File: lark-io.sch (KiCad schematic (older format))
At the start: 30 parts

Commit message: Finalize schematic
Finish part selection

Pending issues: IMU, switches & LEDs, mechanical parts and housing
selection.
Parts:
- C40, C41, C42, C43, C44, C45, C46, C50: renamed from C?; footprint (none) -> Capacitor_SMD:C_0805_2012Metric_Pad1.15x1.40mm_HandSolder; MPN (none) -> 885012207128
- C47: renamed from C?; footprint (none) -> Capacitor_SMD:CP_Elec_16x17.5; MPN (none) -> 493-16063-1-ND
- C48, C49: renamed from C?; footprint (none) -> Capacitor_SMD:C_0805_2012Metric_Pad1.15x1.40mm_HandSolder; MPN (none) -> 885012207102
- F1, F2: renamed from F?; value Polyfuse -> 1.25A/16V; footprint (none) -> Fuse:Fuse_1812_4532Metric_Pad1.30x3.40mm_HandSolder; MPN (none) -> 1812L125/16DR
- J6: renamed from J?; value Conn_01x05 -> UART1; footprint (none) -> Connector_PinHeader_2.54mm:PinHeader_1x05_P2.54mm_Vertical
- J9: renamed from J?; value Conn_01x04 -> SOUND; footprint (none) -> Connector_PinHeader_2.54mm:PinHeader_1x04_P2.54mm_Vertical
- R27, R28, R29, R30, R31, R32: renamed from R?; footprint (none) -> Resistor_SMD:R_0805_2012Metric_Pad1.15x1.40mm_HandSolder; MPN (none) -> RC0805FR-07470RL
- R33, R34: renamed from R?; footprint (none) -> Resistor_SMD:R_0805_2012Metric_Pad1.15x1.40mm_HandSolder; MPN (none) -> RC0805FR-0710KL
- R35, R36: renamed from R?; footprint (none) -> Resistor_SMD:R_0805_2012Metric_Pad1.15x1.40mm_HandSolder; MPN (none) -> RC0805FR-071KL
- U10: renamed from U?; footprint (none) -> Package_SO:SOIC-16_3.9x9.9mm_P1.27mm; MPN (none) -> MAX3232ECDR
- U11: renamed from U?; footprint (none) -> Package_SO:SOIC-16_3.9x9.9mm_P1.27mm; MPN (none) -> PAM8403DR
- gave numbers to parts that had none: 3
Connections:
- no-connect marks 6 -> 7

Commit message: Replace MPU-9250 IMU with BMX055
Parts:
- renumbered C40 to C39, C41 to C40, C42 to C41, C43 to C42, C44 to C43, C45 to C44, C46 to C45, C47 to C46, C48 to C47, C49 to C48, C50 to C49
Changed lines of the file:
@@
 Connection ~ 3750 7200
 $Comp
-L Device:C C42
+L Device:C C41
 U 1 1 5C55CA57
 P 6000 1850
-F 0 "C42" H 6115 1896 50  0000 L CNN
+F 0 "C41" H 6115 1896 50  0000 L CNN
 F 1 "100n" H 6115 1805 50  0000 L CNN
 F 2 "Capacitor_SMD:C_0805_2012Metric_Pad1.15x1.40mm_HandSolder" H 6038 1700 50  0001 C CNN
@@
 $EndComp
 $Comp
-L Device:C C41
+L Device:C C40
 U 1 1 5C55CA9D
 P 3600 1850
-F 0 "C41" H 3715 1896 50  0000 L CNN
+F 0 "C40" H 3715 1896 50  0000 L CNN
 F 1 "100n" H 3715 1805 50  0000 L CNN
 F 2 "Capacitor_SMD:C_0805_2012Metric_Pad1.15x1.40mm_HandSolder" H 3638 1700 50  0001 C CNN
@@
 $EndComp
 $Comp
-L Device:C C40
+L Device:C C39
 U 1 1 5C55CAEA
 P 5250 1000
-F 0 "C40" H 5365 1046 50  0000 L CNN
+F 0 "C39" H 5365 1046 50  0000 L CNN
 F 1 "100n" H 5365 955 50  0000 L CNN
 F 2 "Capacitor_SMD:C_0805_2012Metric_Pad1.15x1.40mm_HandSolder" H 5288 850 50  0001 C CNN
@@
 $EndComp
 $Comp
-L Device:C C43
+L Device:C C42
 U 1 1 5C55CCBE
 P 6400 2200
-F 0 "C43" V 6148 2200 50  0000 C CNN
+F 0 "C42" V 6148 2200 50  0000 C CNN
 F 1 "100n" V 6239 2200 50  0000 C CNN
 F 2 "Capacitor_SMD:C_0805_2012Metric_Pad1.15x1.40mm_HandSolder" H 6438 2050 50  0001 C CNN
@@
 $EndComp
 $Comp
-L Device:C C44
+L Device:C C43
 U 1 1 5C55CF99
 P 6400 2600
-F 0 "C44" V 6148 2600 50  0000 C CNN
+F 0 "C43" V 6148 2600 50  0000 C CNN
 F 1 "100n" V 6239 2600 50  0000 C CNN
 F 2 "Capacitor_SMD:C_0805_2012Metric_Pad1.15x1.40mm_HandSolder" H 6438 2450 50  0001 C CNN
@@
 	3400 4850 3400 5300
 $Comp
-L Device:C C45
+L Device:C C44
 U 1 1 5C5B142F
 P 3050 5100
-F 0 "C45" H 3165 5146 50  0000 L CNN
+F 0 "C44" H 3165 5146 50  0000 L CNN
 F 1 "100n" H 3165 5055 50  0000 L CNN
 F 2 "Capacitor_SMD:C_0805_2012Metric_Pad1.15x1.40mm_HandSolder" H 3088 4950 50  0001 C CNN
@@
 $EndComp
 $Comp
-L Device:C C46
+L Device:C C45
 U 1 1 5C5B14AD
 P 4050 5100
-F 0 "C46" H 4165 5146 50  0000 L CNN
+F 0 "C45" H 4165 5146 50  0000 L CNN
 F 1 "100n" H 4165 5055 50  0000 L CNN
 F 2 "Capacitor_SMD:C_0805_2012Metric_Pad1.15x1.40mm_HandSolder" H 4088 4950 50  0001 C CNN
@@
 $EndComp
 $Comp
-L Device:CP C47
+L Device:CP C46
 U 1 1 5C5BC765
 P 4500 5100
-F 0 "C47" H 4618 5146 50  0000 L CNN
+F 0 "C46" H 4618 5146 50  0000 L CNN
 F 1 "470u" H 4618 5055 50  0000 L CNN
 F 2 "Capacitor_SMD:CP_Elec_16x17.5" H 4538 4950 50  0001 C CNN
@@
 	3050 5250 3050 5350
 $Comp
-L Device:C C48
+L Device:C C47
 U 1 1 5C5FA3E9
 P 2450 5900
-F 0 "C48" V 2198 5900 50  0000 C CNN
+F 0 "C47" V 2198 5900 50  0000 C CNN
 F 1 "470n" V 2289 5900 50  0000 C CNN
 F 2 "Capacitor_SMD:C_0805_2012Metric_Pad1.15x1.40mm_HandSolder" H 2488 5750 50  0001 C CNN
@@
 $EndComp
 $Comp
-L Device:C C49
+L Device:C C48
 U 1 1 5C5FA49A
 P 1900 6200
-F 0 "C49" V 1648 6200 50  0000 C CNN
+F 0 "C48" V 1648 6200 50  0000 C CNN
 F 1 "470n" V 1739 6200 50  0000 C CNN
 F 2 "Capacitor_SMD:C_0805_2012Metric_Pad1.15x1.40mm_HandSolder" H 1938 6050 50  0001 C CNN
@@
 Connection ~ 2750 6350
 $Comp
-L Device:C C50
+L Device:C C49
 U 1 1 5C605E58
 P 2650 6900
-F 0 "C50" H 2765 6946 50  0000 L CNN
+F 0 "C49" H 2765 6946 50  0000 L CNN
 F 1 "100n" H 2765 6855 50  0000 L CNN
 F 2 "Capacitor_SMD:C_0805_2012Metric_Pad1.15x1.40mm_HandSolder" H 2688 6750 50  0001 C CNN

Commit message: Intermediate status while arranging compontents.
Manually grouped components into smaller islands.

Some parts were changed:
* U1: SOT-23-3 LDO should be sufficient
* CP_Elec: Use 10x10 size
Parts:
- C46: footprint Capacitor_SMD:CP_Elec_16x17.5 -> Capacitor_SMD:CP_Elec_10x10
- CON1: symbol dk_Barrel-Audio-Connectors:SJ1-3523N -> lark-rescue:SJ1-3523N-dk_Barrel-Audio-Connectors
- J7, J8: symbol dk_Modular-Connectors-Jacks:54602-908LF -> lark-rescue:54602-908LF-dk_Modular-Connectors-Jacks
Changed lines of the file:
@@
 $EndComp
 $Comp
-L dk_Modular-Connectors-Jacks:54602-908LF J7
+L lark-rescue:54602-908LF-dk_Modular-Connectors-Jacks J7
 U 1 1 5C6D6815
 P 9150 2050
+AR Path="/5C6D6815" Ref="J7"  Part="1"
+AR Path="/5C549AF9/5C6D6815" Ref="J7"  Part="1"
 F 0 "J7" V 9246 1595 50  0000 R CNN
 F 1 "54602-908LF" V 9155 1595 50  0000 R CNN
@@
 $EndComp
 $Comp
-L dk_Modular-Connectors-Jacks:54602-908LF J8
+L lark-rescue:54602-908LF-dk_Modular-Connectors-Jacks J8
 U 1 1 5C6D6947
 P 9150 3550
+AR Path="/5C6D6947" Ref="J8"  Part="1"
+AR Path="/5C549AF9/5C6D6947" Ref="J8"  Part="1"
 F 0 "J8" V 9246 3095 50  0000 R CNN
 F 1 "54602-908LF" V 9155 3095 50  0000 R CNN
@@
 $EndComp
 $Comp
-L dk_Barrel-Audio-Connectors:SJ1-3523N CON1
+L lark-rescue:SJ1-3523N-dk_Barrel-Audio-Connectors CON1
 U 1 1 5C55B74E
 P 5600 6900
+AR Path="/5C55B74E" Ref="CON1"  Part="1"
+AR Path="/5C549AF9/5C55B74E" Ref="CON1"  Part="1"
 F 0 "CON1" H 5273 6953 60  0000 R CNN
 F 1 "SJ1-3523N" H 5273 6847 60  0000 R CNN
@@
 F 0 "C46" H 4618 5146 50  0000 L CNN
 F 1 "470u" H 4618 5055 50  0000 L CNN
-F 2 "Capacitor_SMD:CP_Elec_16x17.5" H 4538 4950 50  0001 C CNN
+F 2 "Capacitor_SMD:CP_Elec_10x10" H 4538 4950 50  0001 C CNN
 F 3 "~" H 4500 5100 50  0001 C CNN
 F 4 "493-16063-1-ND" H 4500 5100 50  0001 C CNN "MPN"

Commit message: continue layout work, WIP
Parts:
- C39, C40, C41, C42, C43, C44, C45, C47, C48, C49: symbol Device:C -> lark-rescue:C-Device
- C46: symbol Device:CP -> lark-rescue:CP-Device
- F1, F2: symbol Device:Polyfuse -> lark-rescue:Polyfuse-Device
- J6: symbol Connector_Generic:Conn_01x05 -> lark-rescue:Conn_01x05-Connector_Generic
- J9: symbol Connector_Generic:Conn_01x04 -> lark-rescue:Conn_01x04-Connector_Generic
- R27, R28, R29, R30, R31, R32, R33, R34, R35, R36: symbol Device:R -> lark-rescue:R-Device
- U10: symbol Interface_UART:MAX3232 -> lark-rescue:MAX3232-Interface_UART
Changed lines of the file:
@@
 $EndComp
 $Comp
-L Interface_UART:MAX3232 U10
+L lark-rescue:MAX3232-Interface_UART U10
 U 1 1 5C6D5FF8
 P 4800 2600
@@
 $EndComp
 $Comp
-L Device:Polyfuse F2
+L lark-rescue:Polyfuse-Device F2
 U 1 1 5C55A114
 P 8300 3250
@@
 $EndComp
 $Comp
-L Device:R R27
+L lark-rescue:R-Device R27
 U 1 1 5C55A24F
 P 1650 2350
@@
 $EndComp
 $Comp
-L Device:R R28
+L lark-rescue:R-Device R28
 U 1 1 5C55A29E
 P 1650 2700
@@
 $EndComp
 $Comp
-L Connector_Generic:Conn_01x04 J9
+L lark-rescue:Conn_01x04-Connector_Generic J9
 U 1 1 5C55B4E7
 P 5700 6000
@@
 NoConn ~ 5500 6800
 $Comp
-L power:GND #PWR050
+L lark-rescue:GND-power #PWR050
 U 1 1 5C55C2EC
 P 3400 7300
@@
 Connection ~ 3750 7200
 $Comp
-L Device:C C41
+L lark-rescue:C-Device C41
 U 1 1 5C55CA57
 P 6000 1850
@@
 $EndComp
 $Comp
-L Device:C C40
+L lark-rescue:C-Device C40
 U 1 1 5C55CA9D
 P 3600 1850
@@
 $EndComp
 $Comp
-L Device:C C39
+L lark-rescue:C-Device C39
 U 1 1 5C55CAEA
 P 5250 1000
@@
 $EndComp
 $Comp
-L power:GND #PWR043
+L lark-rescue:GND-power #PWR043
 U 1 1 5C55CC71
 P 5250 1250
@@
 $EndComp
 $Comp
-L Device:C C42
+L lark-rescue:C-Device C42
 U 1 1 5C55CCBE
 P 6400 2200
@@
 $EndComp
 $Comp
-L Device:C C43
+L lark-rescue:C-Device C43
 U 1 1 5C55CF99
 P 6400 2600
@@
 $EndComp
 $Comp
-L Device:Polyfuse F1
+L lark-rescue:Polyfuse-Device F1
 U 1 1 5C55DC01
 P 8300 1750
@@
 $EndComp
 $Comp
-L power:+12V #PWR044
+L lark-rescue:+12V-power #PWR044
 U 1 1 5C55DEDC
 P 8000 1450
@@
 	8650 3250 8750 3250
 $Comp
-L Connector_Generic:Conn_01x05 J6
+L lark-rescue:Conn_01x05-Connector_Generic J6
 U 1 1 5C55F24D
 P 2550 2050
@@
 $EndComp
 $Comp
-L Device:R R29
+L lark-rescue:R-Device R29
 U 1 1 5C55F619
 P 1650 3050
@@
 $EndComp
 $Comp
-L Device:R R30
+L lark-rescue:R-Device R30
 U 1 1 5C55F6A5
 P 1650 3400
@@
 Connection ~ 2350 2350
 $Comp
-L power:GND #PWR045
+L lark-rescue:GND-power #PWR045
 U 1 1 5C5627B3
 P 2750 2400
@@
 	2750 2250 2750 2400
 $Comp
-L Device:R R31
+L lark-rescue:R-Device R31
 U 1 1 5C56310B
 P 1650 3750
@@
 $EndComp
 $Comp
-L Device:R R32
+L lark-rescue:R-Device R32
 U 1 1 5C5631FD
 P 1650 4100
@@
 	4800 850  4800 1400
 $Comp
-L power:VDD #PWR042
+L lark-rescue:VDD-power #PWR042
 U 1 1 5C56DC3F
 P 4800 850
@@
 Connection ~ 4800 850
 $Comp
-L power:GND #PWR046
+L lark-rescue:GND-power #PWR046
 U 1 1 5C56DCDC
 P 4800 4000
@@
 NoConn ~ 3550 7100
 $Comp
-L power:+5V #PWR047
+L lark-rescue:+5V-power #PWR047
 U 1 1 5C5A9040
 P 3400 4800
@@
 	3400 4850 3400 5300
 $Comp
-L Device:C C44
+L lark-rescue:C-Device C44
 U 1 1 5C5B142F
 P 3050 5100
@@
 $EndComp
 $Comp
-L Device:C C45
+L lark-rescue:C-Device C45
 U 1 1 5C5B14AD
 P 4050 5100
@@
 $EndComp
 $Comp
-L Device:CP C46
+L lark-rescue:CP-Device C46
 U 1 1 5C5BC765
 P 4500 5100
@@
 	4050 4850 4500 4850
 $Comp
-L power:GND #PWR049
+L lark-rescue:GND-power #PWR049
 U 1 1 5C5EF347
 P 4500 5400
@@
 $EndComp
 $Comp
-L power:GND #PWR048
+L lark-rescue:GND-power #PWR048
 U 1 1 5C5EF3AE
 P 3050 5350
@@
 	3050 5250 3050 5350
 $Comp
-L Device:C C47
+L lark-rescue:C-Device C47
 U 1 1 5C5FA3E9
 P 2450 5900
@@
 $EndComp
 $Comp
-L Device:C C48
+L lark-rescue:C-Device C48
 U 1 1 5C5FA49A
 P 1900 6200
@@
 Connection ~ 2750 6350
 $Comp
-L Device:C C49
+L lark-rescue:C-Device C49
 U 1 1 5C605E58
 P 2650 6900
@@
 	2650 7200 3400 7200
 $Comp
-L Device:R R33
+L lark-rescue:R-Device R33
 U 1 1 5C617464
 P 1250 5900
@@
 $EndComp
 $Comp
-L Device:R R34
+L lark-rescue:R-Device R34
 U 1 1 5C617539
 P 1250 6200
@@
 $EndComp
 $Comp
-L Device:R R35
+L lark-rescue:R-Device R35
 U 1 1 5C6175DA
 P 1600 6350
@@
 $EndComp
 $Comp
-L Device:R R36
+L lark-rescue:R-Device R36
 U 1 1 5C6176D6
 P 2200 6500

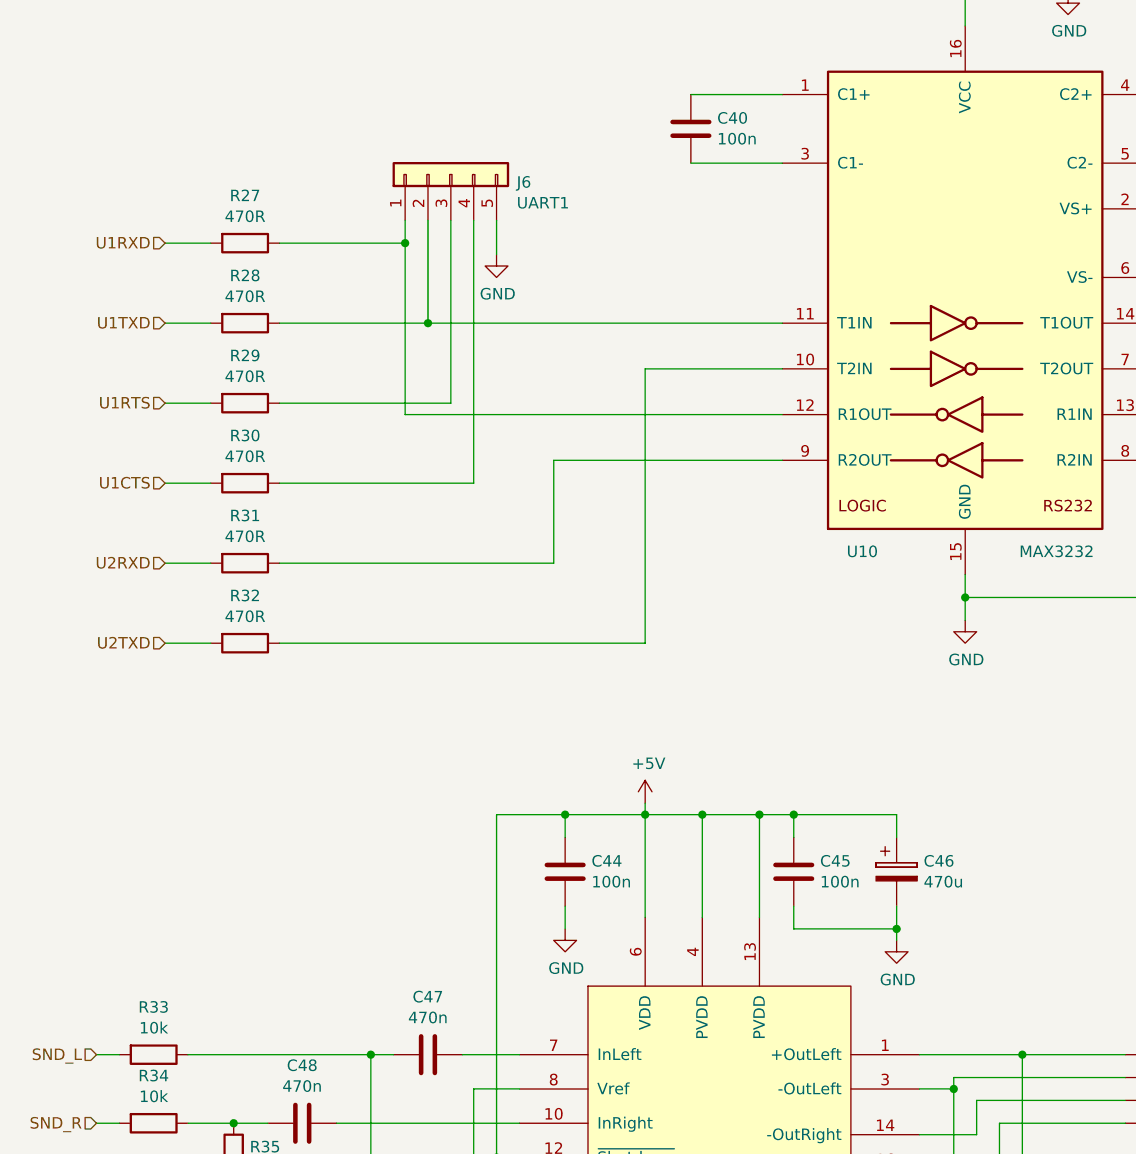
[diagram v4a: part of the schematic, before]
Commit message: Updating schematic for the first prototype
* U1 can supply up to 600 mA
* drop USB charger for now
* smaller type of DC/DC (U2) for input
* remove one of the large capacitors
* change BMX interface to 4-wire SPI for speed reasons
* add I2C mux for pressure sensors

The changes were made during the meeting with Tomas.

BMX055 will be replaced by BMX088. For mechanical reasons, the pressure
sensors will be placed on a daughterboard. The daughterboard could get
footprints for different kinds pressure sensors (i.e. BMP388, HCLA0025).
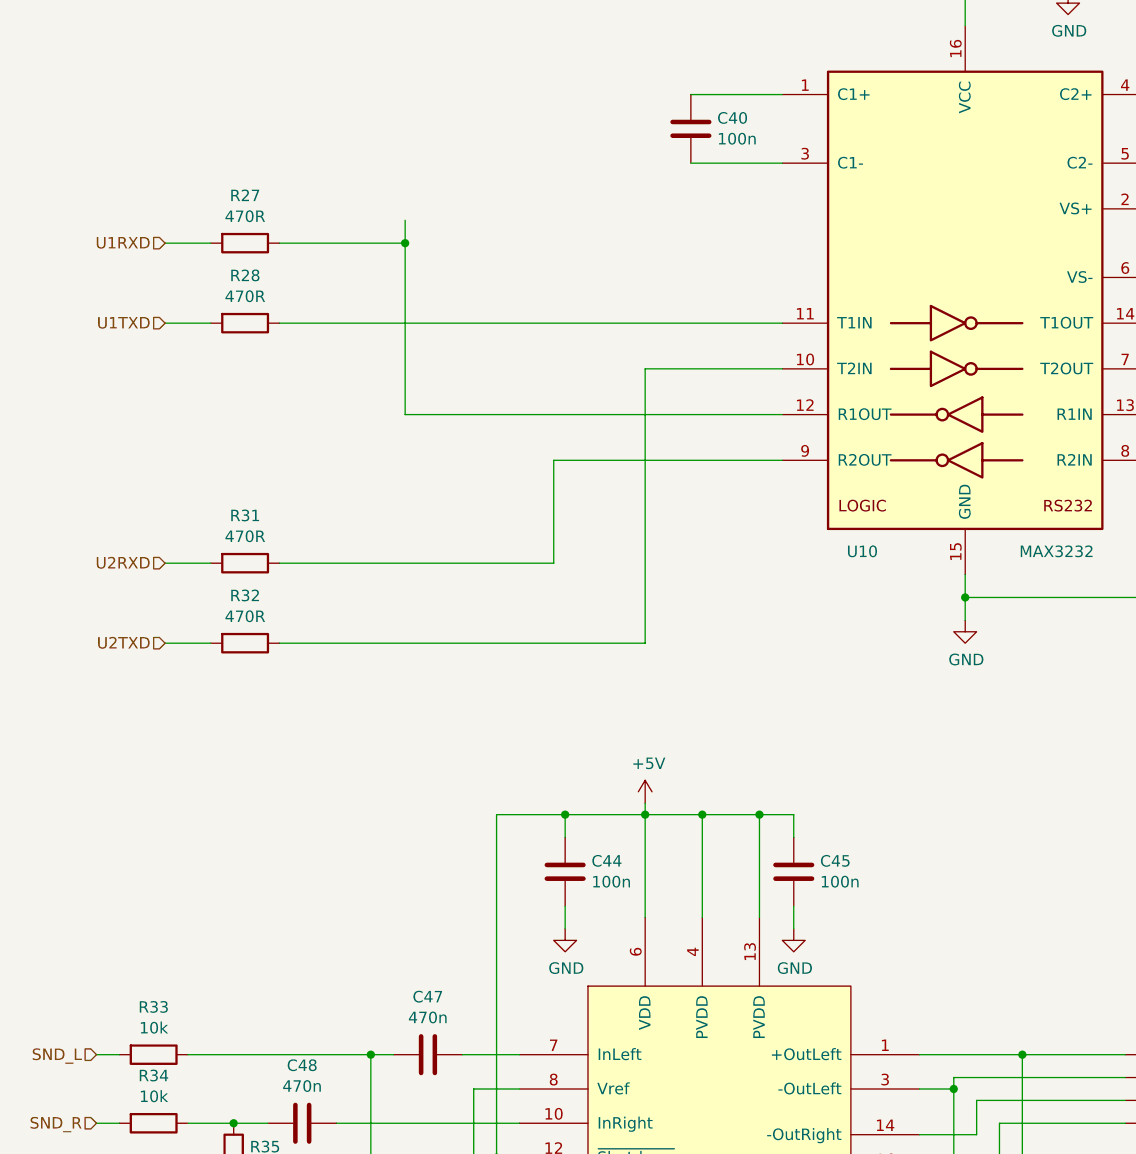
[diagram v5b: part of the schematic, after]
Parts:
- removed C46: 470u, Capacitor_SMD:CP_Elec_10x10, symbol lark-rescue:CP-Device
- removed J6: UART1, Connector_PinHeader_2.54mm:PinHeader_1x05_P2.54mm_Vertical, symbol lark-rescue:Conn_01x05-Connector_Generic
- removed R29, R30: 470R, Resistor_SMD:R_0805_2012Metric_Pad1.15x1.40mm_HandSolder, symbol lark-rescue:R-Device

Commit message: Use BMI088 instead of BMX055.
Symbol for BMI088 was created and placed in the schematic.

Still looking for a LGA-16 4.5x3.0 footprint. Do we really need to
create that ourselves?
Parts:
- J7, J8: footprint digikey-footprints:Ethernet_Jack_54602-908LF -> libs:634108185521
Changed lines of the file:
@@
 F 0 "J7" V 9246 1595 50  0000 R CNN
 F 1 "54602-908LF" V 9155 1595 50  0000 R CNN
-F 2 "digikey-footprints:Ethernet_Jack_54602-908LF" H 9350 2250 50  0001 L CNN
+F 2 "libs:634108185521" H 9350 2250 50  0001 L CNN
 F 3 "" H 9350 2350 60  0001 L CNN
 F 4 "609-1046-ND" H 9350 2450 60  0001 L CNN "Digi-Key_PN"
@@
 F 0 "J8" V 9246 3095 50  0000 R CNN
 F 1 "54602-908LF" V 9155 3095 50  0000 R CNN
-F 2 "digikey-footprints:Ethernet_Jack_54602-908LF" H 9350 3750 50  0001 L CNN
+F 2 "libs:634108185521" H 9350 3750 50  0001 L CNN
 F 3 "" H 9350 3850 60  0001 L CNN
 F 4 "609-1046-ND" H 9350 3950 60  0001 L CNN "Digi-Key_PN"

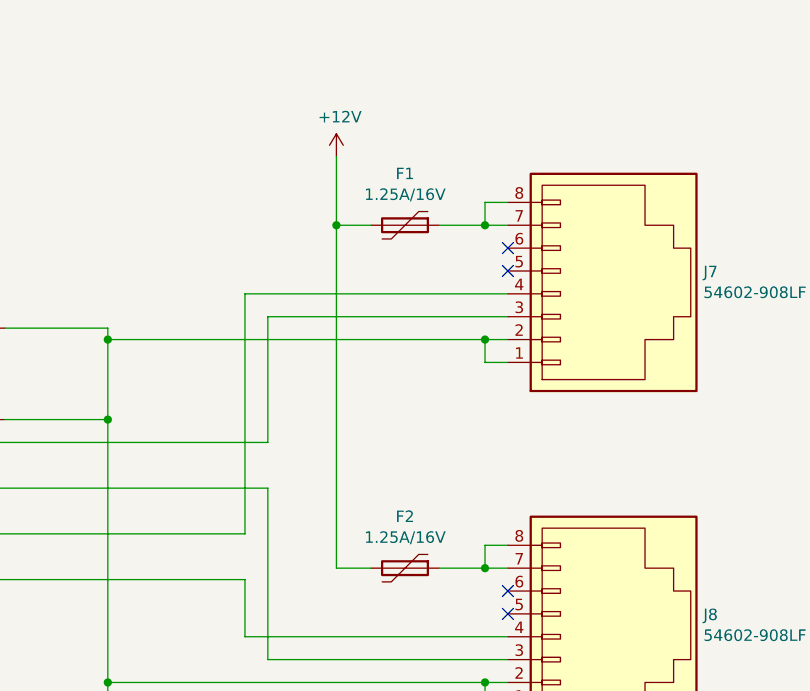
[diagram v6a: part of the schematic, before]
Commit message: Fitting layout into 57 mm instrument.
* board width is 51 mm at the moment
* split into two boards (sensor and main) which can be stacked with
  2.54 mm pinheaders.
* ESP32 was put to bottom with optional pcb antenna facing to front.
* added footprint for optional HCLAxxE on sensorboard
* added footprint for BMI088

* Is multiple GND pins for sensor board really a good idea (ground loops)?
* Does the +12V topology make sense (especially regarding the external
  IGC ports)?
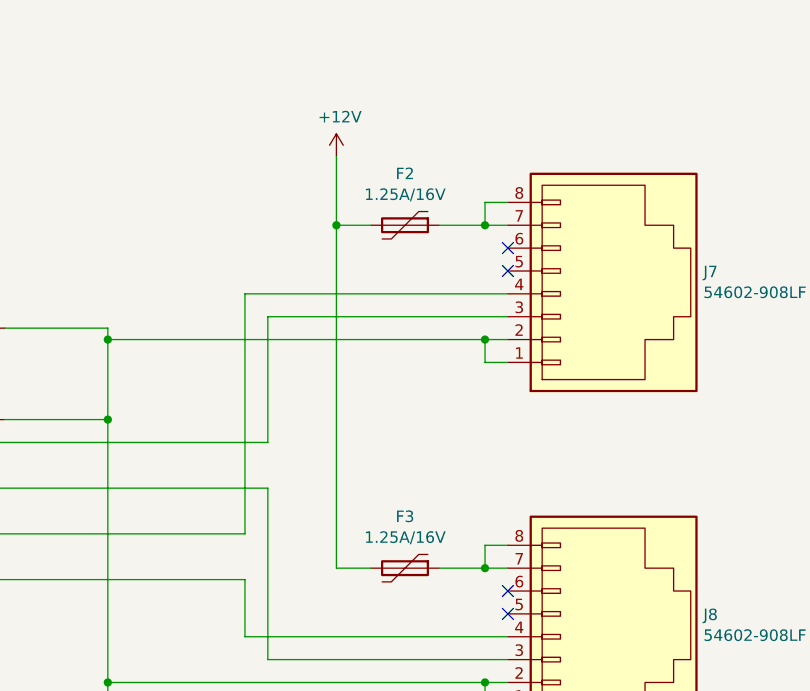
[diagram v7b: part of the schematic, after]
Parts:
- renumbered F1 to F2, F2 to F3
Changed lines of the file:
@@
 $EndComp
 $Comp
-L lark-rescue:Polyfuse-Device F2
+L lark-rescue:Polyfuse-Device F3
 U 1 1 5C55A114
 P 8300 3250
-F 0 "F2" V 8075 3250 50  0000 C CNN
+F 0 "F3" V 8075 3250 50  0000 C CNN
 F 1 "1.25A/16V" V 8166 3250 50  0000 C CNN
 F 2 "Fuse:Fuse_1812_4532Metric_Pad1.30x3.40mm_HandSolder" H 8350 3050 50  0001 L CNN
@@
 $EndComp
 $Comp
-L lark-rescue:Polyfuse-Device F1
+L lark-rescue:Polyfuse-Device F2
 U 1 1 5C55DC01
 P 8300 1750
-F 0 "F1" V 8075 1750 50  0000 C CNN
+F 0 "F2" V 8075 1750 50  0000 C CNN
 F 1 "1.25A/16V" V 8166 1750 50  0000 C CNN
 F 2 "Fuse:Fuse_1812_4532Metric_Pad1.30x3.40mm_HandSolder" H 8350 1550 50  0001 L CNN
